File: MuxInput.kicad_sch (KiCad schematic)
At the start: 0 parts

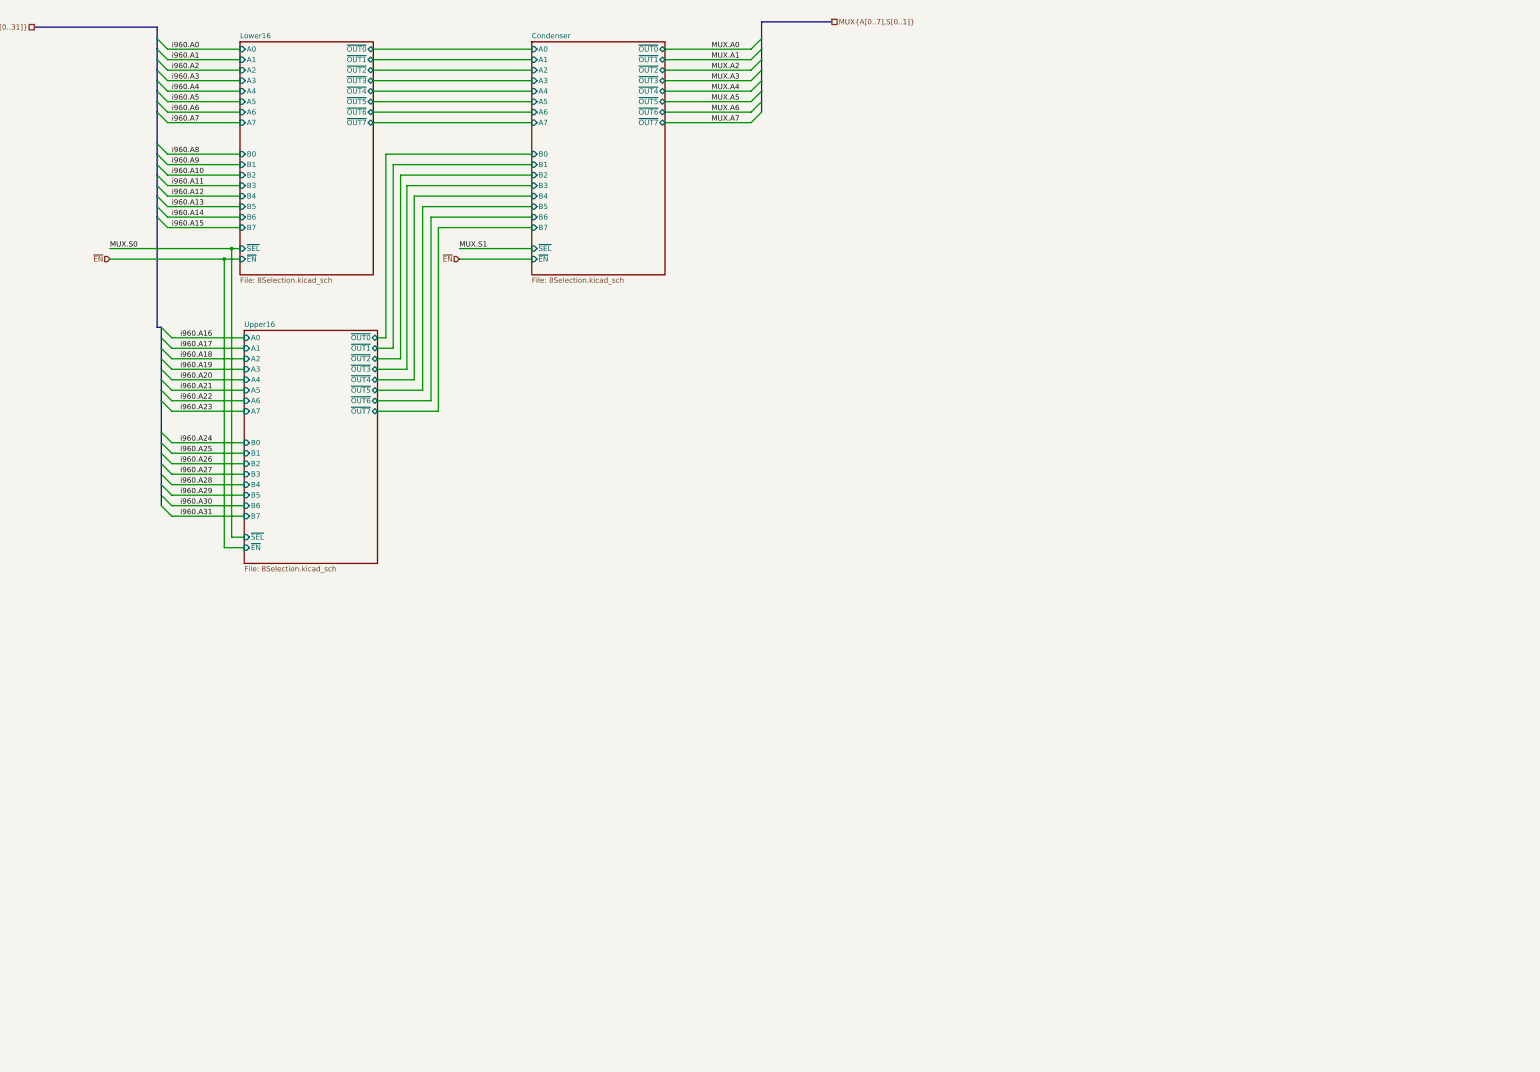
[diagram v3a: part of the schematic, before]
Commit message: Use AHC244s instead of AHC158s for the address lines
Makes it much easier to design the selection bus!
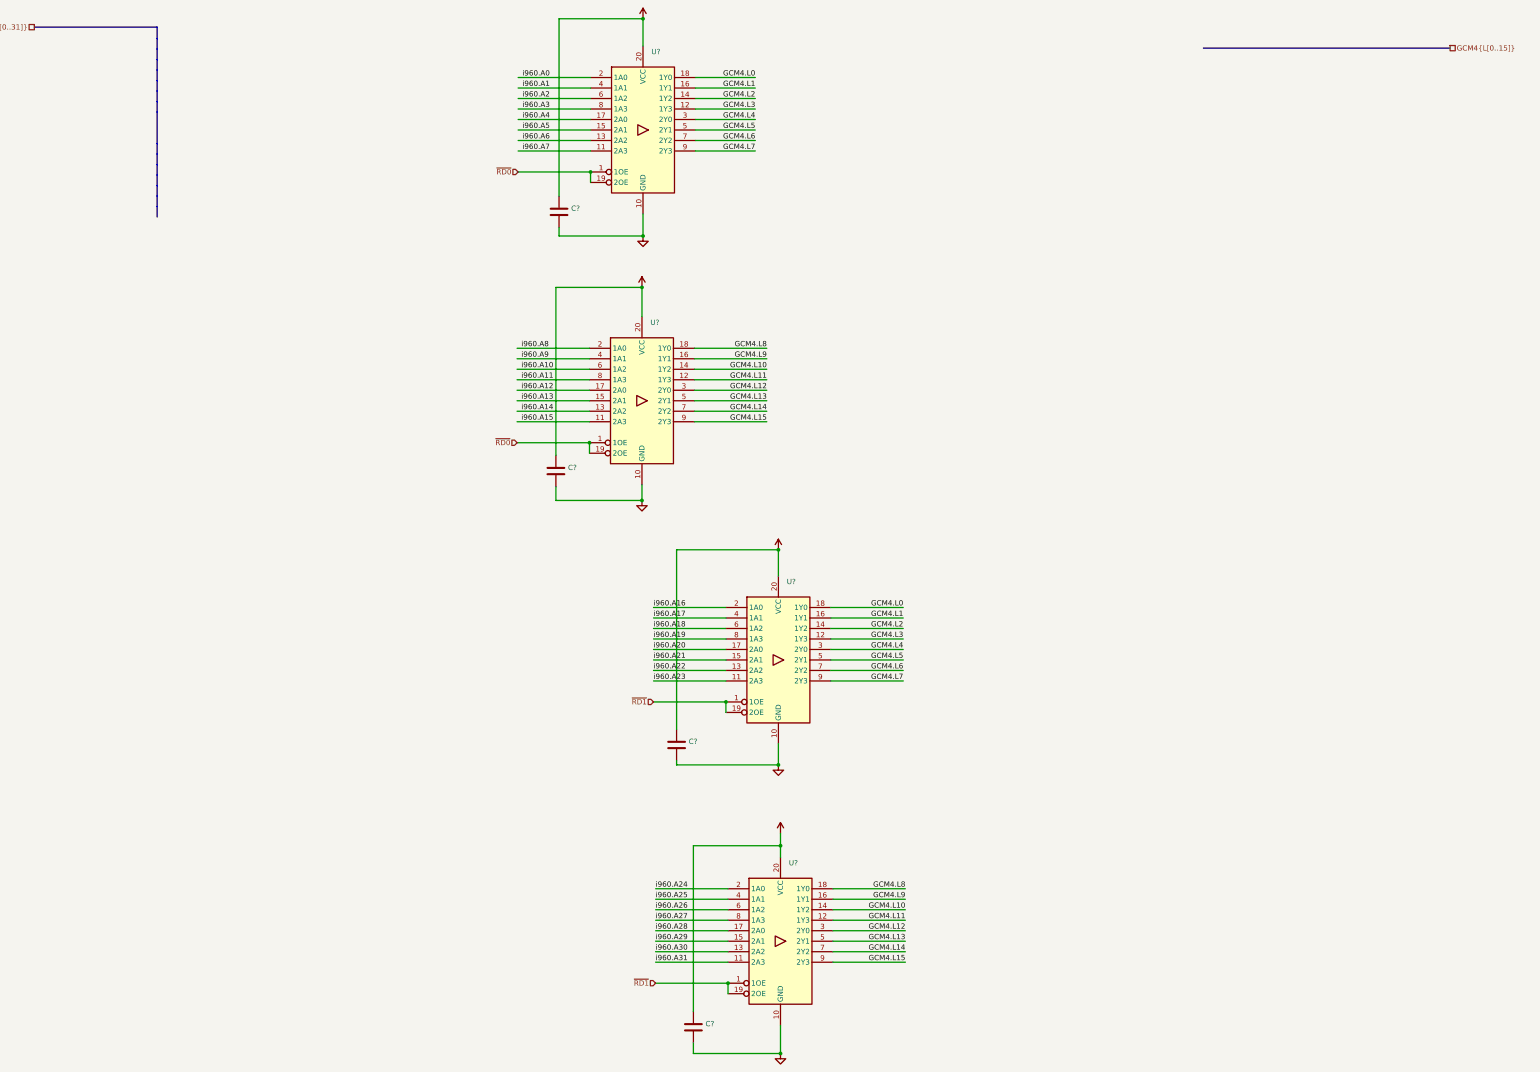
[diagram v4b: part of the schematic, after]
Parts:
- added C? (x4): (no value), symbol Device:C
- added U? (x4): (no value), symbol 74xx:74HC244
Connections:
- net i960.A0: now also U?.2 (1A0)
- net i960.A1: now also U?.4 (1A1)
- net i960.A10: now also U?.6 (1A2)
- net i960.A11: now also U?.8 (1A3)
- net i960.A12: now also U?.17 (2A0)
- net i960.A13: now also U?.15 (2A1)
- net i960.A14: now also U?.13 (2A2)
- net i960.A15: now also U?.11 (2A3)
- net i960.A16: now also U?.2 (1A0)
- net i960.A17: now also U?.4 (1A1)
- net i960.A18: now also U?.6 (1A2)
- net i960.A19: now also U?.8 (1A3)
- net i960.A2: now also U?.6 (1A2)
- net i960.A20: now also U?.17 (2A0)
- net i960.A21: now also U?.15 (2A1)
- net i960.A22: now also U?.13 (2A2)
- net i960.A23: now also U?.11 (2A3)
- net i960.A24: now also U?.2 (1A0)
- net i960.A25: now also U?.4 (1A1)
- net i960.A26: now also U?.6 (1A2)
- net i960.A27: now also U?.8 (1A3)
- net i960.A28: now also U?.17 (2A0)
- net i960.A29: now also U?.15 (2A1)
- net i960.A3: now also U?.8 (1A3)
- net i960.A30: now also U?.13 (2A2)
- net i960.A31: now also U?.11 (2A3)
- net i960.A4: now also U?.17 (2A0)
- net i960.A5: now also U?.15 (2A1)
- net i960.A6: now also U?.13 (2A2)
- net i960.A7: now also U?.11 (2A3)
- net i960.A8: now also U?.2 (1A0)
- net i960.A9: now also U?.4 (1A1)
- new net GCM4.L0: U?.18 (1Y0), U?.18 (1Y0)
- new net GCM4.L1: U?.16 (1Y1), U?.16 (1Y1)
- new net GCM4.L10: U?.14 (1Y2), U?.14 (1Y2)
- new net GCM4.L11: U?.12 (1Y3), U?.12 (1Y3)
- new net GCM4.L12: U?.3 (2Y0), U?.3 (2Y0)
- new net GCM4.L13: U?.5 (2Y1), U?.5 (2Y1)
- new net GCM4.L14: U?.7 (2Y2), U?.7 (2Y2)
- new net GCM4.L15: U?.9 (2Y3), U?.9 (2Y3)
- new net GCM4.L2: U?.14 (1Y2), U?.14 (1Y2)
- new net GCM4.L3: U?.12 (1Y3), U?.12 (1Y3)
- new net GCM4.L4: U?.3 (2Y0), U?.3 (2Y0)
- new net GCM4.L5: U?.5 (2Y1), U?.5 (2Y1)
- new net GCM4.L6: U?.7 (2Y2), U?.7 (2Y2)
- new net GCM4.L7: U?.9 (2Y3), U?.9 (2Y3)
- new net GCM4.L8: U?.18 (1Y0), U?.18 (1Y0)
- new net GCM4.L9: U?.16 (1Y1), U?.16 (1Y1)
- new net GND: C?.2, C?.2, C?.2, C?.2, U?.10 (GND), U?.10 (GND), U?.10 (GND), U?.10 (GND)
- new net VCC: C?.1, C?.1, C?.1, C?.1, U?.20 (VCC), U?.20 (VCC), U?.20 (VCC), U?.20 (VCC)
- new net ~{RD0}: U?.1 (1OE), U?.1 (1OE), U?.19 (2OE), U?.19 (2OE)
- new net ~{RD1}: U?.1 (1OE), U?.1 (1OE), U?.19 (2OE), U?.19 (2OE)
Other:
- removed sheet Condenser
- removed sheet Lower16
- removed sheet Upper16

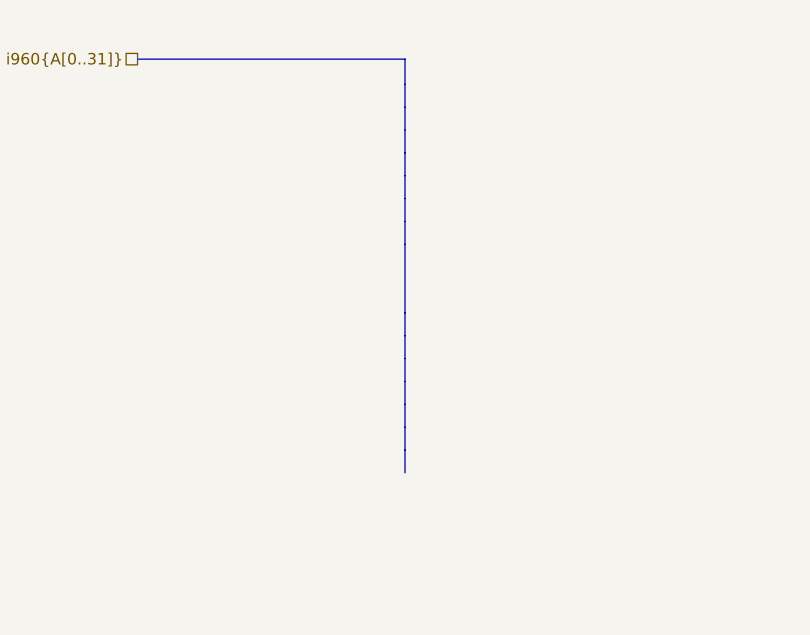
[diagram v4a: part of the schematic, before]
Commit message: Use an AHC138/HC138 for decoding the fail circuit
It is much simpler this way. I can also use the other states to define
the actions to perform.
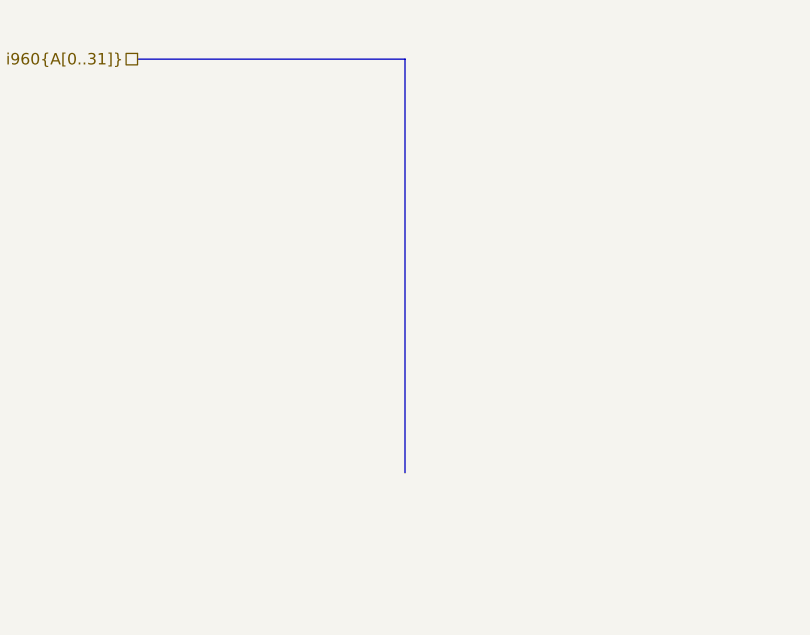
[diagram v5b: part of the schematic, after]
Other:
- title: (none) -> Address Lines Interface
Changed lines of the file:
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@@
   (paper "A3")
   (title_block
+    (title "Address Lines Interface")
     (date "2022-05-13")
     (rev "1")
     (company "Joshua Scoggins")
+    (comment 1 "Performs tri-stating and logic level conversion of address lines")
+    (comment 2 "Implicitly one way design from i960 domain to chipset domain")
   )
   (junction (at 214.884 272.034) (diameter 0) (color 0 0 0 0)
@@
     (stroke (width 0) (type default) (color 0 0 0 0))
   )
-  (bus (pts (xy 64.008 67.056) (xy 64.008 69.596))
-    (stroke (width 0) (type default) (color 0 0 0 0))
-  )
   (wire (pts (xy 194.056 103.886) (xy 211.582 103.886))
     (stroke (width 0) (type default) (color 0 0 0 0))
   )
-  (bus (pts (xy 64.008 34.036) (xy 64.008 36.576))
-    (stroke (width 0) (type default) (color 0 0 0 0))
-  )
-  (bus (pts (xy 64.008 54.356) (xy 64.008 56.896))
-    (stroke (width 0) (type default) (color 0 0 0 0))
-  )
   (wire (pts (xy 214.376 150.114) (xy 189.738 150.114))
     (stroke (width 0) (type default) (color 0 0 0 0))
@@
     (stroke (width 0) (type default) (color 0 0 0 0))
   )
-  (bus (pts (xy 64.008 23.622) (xy 64.008 26.416))
-    (stroke (width 0) (type default) (color 0 0 0 0))
-  )
   (wire (pts (xy 194.31 45.974) (xy 208.788 45.974))
     (stroke (width 0) (type default) (color 0 0 0 0))
@@
     (stroke (width 0) (type default) (color 0 0 0 0))
   )
-  (bus (pts (xy 64.008 56.896) (xy 64.008 59.436))
-    (stroke (width 0) (type default) (color 0 0 0 0))
-  )
   (wire (pts (xy 168.91 58.674) (xy 168.91 61.214))
     (stroke (width 0) (type default) (color 0 0 0 0))
@@
     (stroke (width 0) (type default) (color 0 0 0 0))
   )
-  (bus (pts (xy 64.008 31.496) (xy 64.008 34.036))
-    (stroke (width 0) (type default) (color 0 0 0 0))
-  )
   (wire (pts (xy 184.658 255.016) (xy 202.184 255.016))
     (stroke (width 0) (type default) (color 0 0 0 0))
@@
     (stroke (width 0) (type default) (color 0 0 0 0))
   )
-  (bus (pts (xy 64.008 59.436) (xy 64.008 61.976))
-    (stroke (width 0) (type default) (color 0 0 0 0))
-  )
   (wire (pts (xy 194.31 53.594) (xy 208.788 53.594))
     (stroke (width 0) (type default) (color 0 0 0 0))
@@
     (stroke (width 0) (type default) (color 0 0 0 0))
   )
-  (bus (pts (xy 64.008 51.816) (xy 64.008 54.356))
-    (stroke (width 0) (type default) (color 0 0 0 0))
-  )
   (wire (pts (xy 151.384 58.674) (xy 168.91 58.674))
     (stroke (width 0) (type default) (color 0 0 0 0))
@@
     (stroke (width 0) (type default) (color 0 0 0 0))
   )
-  (bus (pts (xy 64.008 28.956) (xy 64.008 31.496))
-    (stroke (width 0) (type default) (color 0 0 0 0))
-  )
   (wire (pts (xy 184.15 169.164) (xy 201.676 169.164))
     (stroke (width 0) (type default) (color 0 0 0 0))
@@
     (stroke (width 0) (type default) (color 0 0 0 0))
   )
-  (bus (pts (xy 64.008 26.416) (xy 64.008 28.956))
-    (stroke (width 0) (type default) (color 0 0 0 0))
-  )
   (wire (pts (xy 194.056 114.046) (xy 211.582 114.046))
     (stroke (width 0) (type default) (color 0 0 0 0))
@@
     (stroke (width 0) (type default) (color 0 0 0 0))
   )
-  (bus (pts (xy 64.008 39.116) (xy 64.008 41.656))
-    (stroke (width 0) (type default) (color 0 0 0 0))
-  )
   (wire (pts (xy 227.584 239.776) (xy 245.11 239.776))
     (stroke (width 0) (type default) (color 0 0 0 0))
   )
-  (bus (pts (xy 64.008 44.196) (xy 64.008 51.816))
+  (bus (pts (xy 64.008 23.622) (xy 64.008 69.596))
     (stroke (width 0) (type default) (color 0 0 0 0))
   )
@@
     (stroke (width 0) (type default) (color 0 0 0 0))
   )
-  (bus (pts (xy 64.008 64.516) (xy 64.008 67.056))
-    (stroke (width 0) (type default) (color 0 0 0 0))
-  )
   (wire (pts (xy 194.056 101.346) (xy 211.582 101.346))
     (stroke (width 0) (type default) (color 0 0 0 0))
   )
-  (bus (pts (xy 64.008 41.656) (xy 64.008 44.196))
-    (stroke (width 0) (type default) (color 0 0 0 0))
-  )
   (wire (pts (xy 227.584 249.936) (xy 245.11 249.936))
     (stroke (width 0) (type default) (color 0 0 0 0))
@@
     (stroke (width 0) (type default) (color 0 0 0 0))
   )
-  (bus (pts (xy 64.008 61.976) (xy 64.008 64.516))
-    (stroke (width 0) (type default) (color 0 0 0 0))
-  )
-  (bus (pts (xy 64.008 36.576) (xy 64.008 39.116))
-    (stroke (width 0) (type default) (color 0 0 0 0))
-  )

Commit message: Initial layout complete
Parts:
- gave numbers to parts that had none: 8
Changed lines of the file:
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@@
   (symbol (lib_id "power:GND") (at 181.356 138.176 0) (unit 1)
     (in_bom yes) (on_board yes) (fields_autoplaced)
-    (property "Reference" "#PWR?" (id 0) (at 181.356 144.526 0)
+    (property "Reference" "#PWR0110" (id 0) (at 181.356 144.526 0)
       (effects (font (size 1.27 1.27)) hide)
     )
@@
   (symbol (lib_id "power:VCC") (at 214.884 218.694 0) (unit 1)
     (in_bom yes) (on_board yes) (fields_autoplaced)
-    (property "Reference" "#PWR?" (id 0) (at 214.884 222.504 0)
+    (property "Reference" "#PWR0115" (id 0) (at 214.884 222.504 0)
       (effects (font (size 1.27 1.27)) hide)
     )
@@
   (symbol (lib_id "Device:C") (at 161.29 68.326 0) (unit 1)
     (in_bom yes) (on_board yes) (fields_autoplaced)
-    (property "Reference" "C?" (id 0) (at 164.211 67.4913 0)
+    (property "Reference" "C3" (id 0) (at 164.211 67.4913 0)
       (effects (font (size 1.27 1.27)) (justify left))
     )
@@
   (symbol (lib_id "74xx:74HC244") (at 181.356 114.046 0) (unit 1)
     (in_bom yes) (on_board yes) (fields_autoplaced)
-    (property "Reference" "U?" (id 0) (at 183.3754 95.1062 0)
+    (property "Reference" "U2" (id 0) (at 183.3754 95.1062 0)
       (effects (font (size 1.27 1.27)) (justify left))
     )
@@
   (symbol (lib_id "power:VCC") (at 181.61 21.59 0) (unit 1)
     (in_bom yes) (on_board yes) (fields_autoplaced)
-    (property "Reference" "#PWR?" (id 0) (at 181.61 25.4 0)
+    (property "Reference" "#PWR0109" (id 0) (at 181.61 25.4 0)
       (effects (font (size 1.27 1.27)) hide)
     )
@@
   (symbol (lib_id "power:GND") (at 181.61 74.168 0) (unit 1)
     (in_bom yes) (on_board yes) (fields_autoplaced)
-    (property "Reference" "#PWR?" (id 0) (at 181.61 80.518 0)
+    (property "Reference" "#PWR0113" (id 0) (at 181.61 80.518 0)
       (effects (font (size 1.27 1.27)) hide)
     )
@@
   (symbol (lib_id "power:VCC") (at 214.376 150.114 0) (unit 1)
     (in_bom yes) (on_board yes) (fields_autoplaced)
-    (property "Reference" "#PWR?" (id 0) (at 214.376 153.924 0)
+    (property "Reference" "#PWR0114" (id 0) (at 214.376 153.924 0)
       (effects (font (size 1.27 1.27)) hide)
     )
@@
   (symbol (lib_id "Device:C") (at 160.528 131.064 0) (unit 1)
     (in_bom yes) (on_board yes) (fields_autoplaced)
-    (property "Reference" "C?" (id 0) (at 163.449 130.2293 0)
+    (property "Reference" "C2" (id 0) (at 163.449 130.2293 0)
       (effects (font (size 1.27 1.27)) (justify left))
     )
@@
   (symbol (lib_id "power:VCC") (at 181.356 86.614 0) (unit 1)
     (in_bom yes) (on_board yes) (fields_autoplaced)
-    (property "Reference" "#PWR?" (id 0) (at 181.356 90.424 0)
+    (property "Reference" "#PWR0112" (id 0) (at 181.356 90.424 0)
       (effects (font (size 1.27 1.27)) hide)
     )
@@
   (symbol (lib_id "74xx:74HC244") (at 214.884 244.856 0) (unit 1)
     (in_bom yes) (on_board yes) (fields_autoplaced)
-    (property "Reference" "U?" (id 0) (at 216.9034 225.9162 0)
+    (property "Reference" "U5" (id 0) (at 216.9034 225.9162 0)
       (effects (font (size 1.27 1.27)) (justify left))
     )
@@
   (symbol (lib_id "power:GND") (at 214.376 202.184 0) (unit 1)
     (in_bom yes) (on_board yes) (fields_autoplaced)
-    (property "Reference" "#PWR?" (id 0) (at 214.376 208.534 0)
+    (property "Reference" "#PWR0116" (id 0) (at 214.376 208.534 0)
       (effects (font (size 1.27 1.27)) hide)
     )
@@
   (symbol (lib_id "74xx:74HC244") (at 181.61 48.514 0) (unit 1)
     (in_bom yes) (on_board yes) (fields_autoplaced)
-    (property "Reference" "U?" (id 0) (at 183.6294 29.5742 0)
+    (property "Reference" "U3" (id 0) (at 183.6294 29.5742 0)
       (effects (font (size 1.27 1.27)) (justify left))
     )
@@
   (symbol (lib_id "power:GND") (at 214.884 272.034 0) (unit 1)
     (in_bom yes) (on_board yes) (fields_autoplaced)
-    (property "Reference" "#PWR?" (id 0) (at 214.884 278.384 0)
+    (property "Reference" "#PWR0111" (id 0) (at 214.884 278.384 0)
       (effects (font (size 1.27 1.27)) hide)
     )
@@
   (symbol (lib_id "74xx:74HC244") (at 214.376 176.784 0) (unit 1)
     (in_bom yes) (on_board yes) (fields_autoplaced)
-    (property "Reference" "U?" (id 0) (at 216.3954 157.8442 0)
+    (property "Reference" "U4" (id 0) (at 216.3954 157.8442 0)
       (effects (font (size 1.27 1.27)) (justify left))
     )
@@
   (symbol (lib_id "Device:C") (at 193.802 265.684 0) (unit 1)
     (in_bom yes) (on_board yes) (fields_autoplaced)
-    (property "Reference" "C?" (id 0) (at 196.723 264.8493 0)
+    (property "Reference" "C5" (id 0) (at 196.723 264.8493 0)
       (effects (font (size 1.27 1.27)) (justify left))
     )
@@
   (symbol (lib_id "Device:C") (at 189.738 197.358 0) (unit 1)
     (in_bom yes) (on_board yes) (fields_autoplaced)
-    (property "Reference" "C?" (id 0) (at 192.659 196.5233 0)
-      (effects (font (size 1.27 1.27)) (justify left))
-    )
+    (property "Reference" "C4" (id 0) (at 192.659 196.5233 0)
+      (effects (font (size 1.27 1.27)) (justify left))
+    )
